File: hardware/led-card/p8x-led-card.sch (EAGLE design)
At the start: 19 parts, among them J1 MABC96R, U1 74HCT30, U2 74HCT138, U3 74HCT138, U4 74HCT32, U5 74HCT14, U6 74HCT374

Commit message: feat(hardware): 100nF bypass caps to 0.1" lead pitch on all boards
The 100nF ceramic-disc decoupling/bypass caps used the shared C_DISC footprint
at 0.2" (5.08mm) lead spacing. The parts being sourced are 0.1" (2.54mm) pitch,
so retarget just those caps:

- Add a C_DISC1 footprint (pad 2 at y=-2.54) and a CAP1 device that reuses the
  CAP schematic symbol art but points at C_DISC1.
- Route the 100nF parts to CAP1: per-IC decoupling (CDn), the placement-flow
  copies, and the backplane per-slot caps C1-C10.
- Leave C_DISC (0.2") for the parts that still use it: the 1uF caps, the 150pF
  clock terminators (CT1/CT2), and the XTAL32 placeholder.

Regenerated all 8 boards (.sch/.brd/-full.brd) and the schematic PDFs; the
narrower pad field also relieves the backplane connector clearance. Validation:
0 errors on all boards.

Co-Authored-By: Claude Opus 4.8 <noreply@anthropic.com>
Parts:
- CD1, CD2, CD3, CD4, CD5, CD6: device p8x:CAP -> p8x:CAP1
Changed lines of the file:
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@@
 <part name="R4" library="p8x" deviceset="RES" device="" value="1K"/>
 <part name="LED4" library="p8x" deviceset="LED" device="" value="YEL"/>
-<part name="CD1" library="p8x" deviceset="CAP" device="" value="100N"/>
-<part name="CD2" library="p8x" deviceset="CAP" device="" value="100N"/>
-<part name="CD3" library="p8x" deviceset="CAP" device="" value="100N"/>
-<part name="CD4" library="p8x" deviceset="CAP" device="" value="100N"/>
-<part name="CD5" library="p8x" deviceset="CAP" device="" value="100N"/>
-<part name="CD6" library="p8x" deviceset="CAP" device="" value="100N"/>
+<part name="CD1" library="p8x" deviceset="CAP1" device="" value="100N"/>
+<part name="CD2" library="p8x" deviceset="CAP1" device="" value="100N"/>
+<part name="CD3" library="p8x" deviceset="CAP1" device="" value="100N"/>
+<part name="CD4" library="p8x" deviceset="CAP1" device="" value="100N"/>
+<part name="CD5" library="p8x" deviceset="CAP1" device="" value="100N"/>
+<part name="CD6" library="p8x" deviceset="CAP1" device="" value="100N"/>
 </parts><sheets><sheet><plain>
 <text x="0" y="40" size="3.81" layer="97">P8X LED OUTPUT CARD (test - write-only 8 LEDs at $FF0C)</text>

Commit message: fix(gen_eagle): card J1 schematic footprint was FABC96S (female), should be MABC96R
Spotted on the bustest board review: J1, the card edge connector, showed as
FABC96S in the schematic — the female VERTICAL backplane socket — when a card
mates as the MALE right-angle MABC96R. card() bound the schematic J1 to deviceset
DIN96 (FABC96S) while the board bound DIN96C (MABC96R): a schematic/board
footprint mismatch present on EVERY card, not just bustest.

The physical result was never wrong — the generator bakes identical pad geometry
for both names (verified: MABC96R and FABC96S have byte-identical pad maps in
con-vg too), so boards were always correct. But the schematic labelled the card
connector as the backplane socket, which is what the review caught, and it breaks
schematic/board consistency.

One-line fix: schematic J1 now binds DIN96C -> MABC96R, matching the board. The
backplane keeps DIN96/FABC96S for its own slots — those ARE the female sockets;
only cards are male. All 8 existing card schematics get the same correction (they
shared the bug); the backplane schematic and every .brd are unchanged.

Regenerated the 9 affected schematic PDFs to match; reverted placement-PDF and
backplane-PDF timestamp churn.

Co-Authored-By: Claude Opus 4.8 <noreply@anthropic.com>
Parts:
- J1: device p8x:DIN96 -> p8x:DIN96C
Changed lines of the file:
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@@
 <classes><class number="0" name="default" width="0" drill="0"/></classes>
 <parts>
-<part name="J1" library="p8x" deviceset="DIN96" device="" value="MABC96R"/>
+<part name="J1" library="p8x" deviceset="DIN96C" device="" value="MABC96R"/>
 <part name="U1" library="p8x" deviceset="7430" device="" value="74HCT30"/>
 <part name="U2" library="p8x" deviceset="74138" device="" value="74HCT138"/>

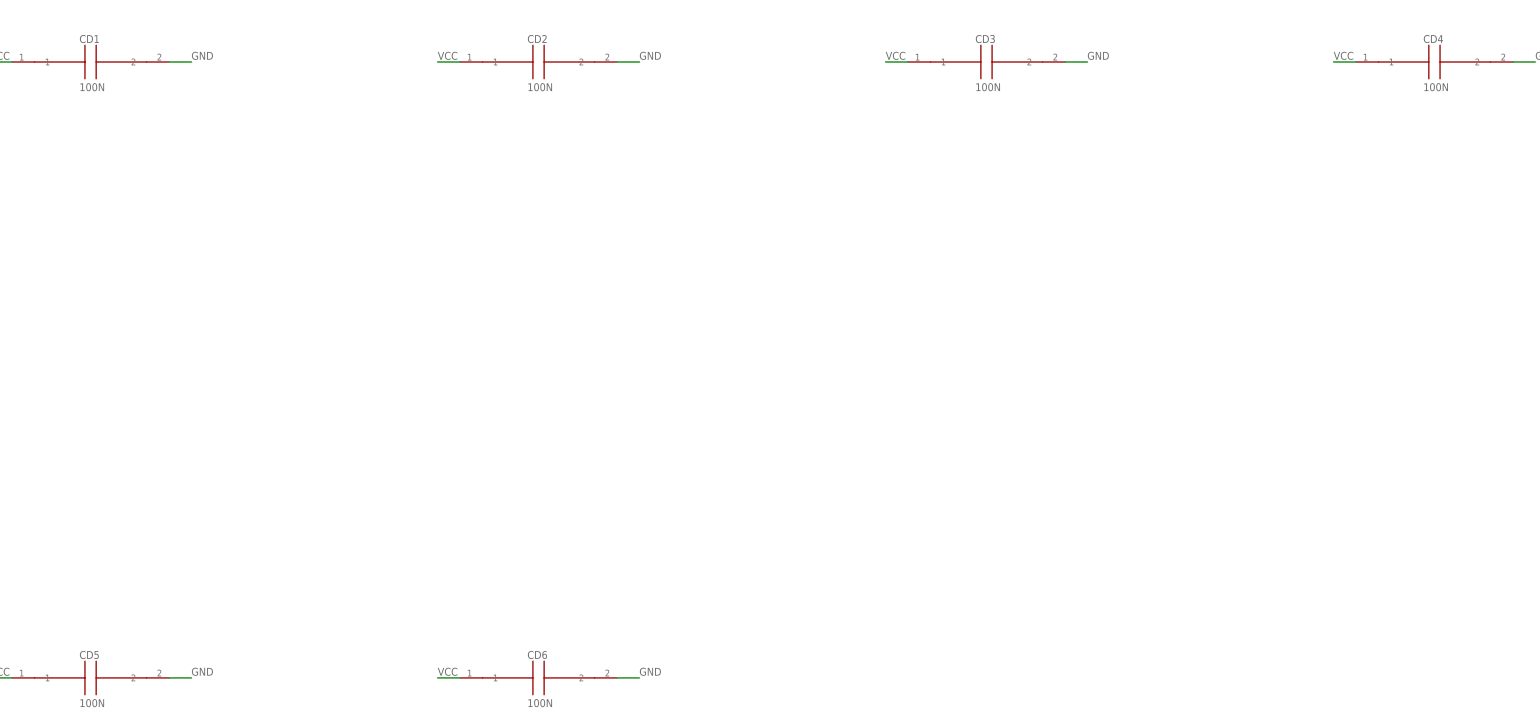
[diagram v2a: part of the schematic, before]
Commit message: hardware: silkscreen off footprints, standard cap value format, backplane RL1->R1
Pre-Fusion cleanup so there is less to fix by hand once placing/routing.

1. SILKSCREEN NO LONGER OVERLAYS FOOTPRINTS (all boards). NAME/VALUE were emitted
   at the element origin +/-2.54 regardless of part size, so on anything bigger
   than a 2-pin part the text landed ON the pads -- the 96-pin DIN connector had
   J1/SLOT1 across its pad field, and caps had their values on top of them. Now
   placed against the real footprint bbox (fp_box): NAME 0.7mm above the top edge,
   VALUE 0.7mm below the bottom, left-aligned to the box. Verified: 1642
   silkscreen labels across all 9 boards, 0 sitting on a footprint (was many).
   Not rotation-aware, which is fine -- no board rotates a part today.

2. CAPACITOR VALUES use standard unit suffixes: 100N->100nF, 470U->470uF,
   150P->150pF, 1U->1uF (and the DNP/x10 variants). Applied everywhere, so the
   per-IC decoupling caps on every card change too. No doc quoted the raw value
   strings, so no doc churn.

3. BACKPLANE RL1 -> R1 (standard R designator). Scoped to the backplane section
   only -- the io-card and led-card have their own unrelated RL1 (8x330R networks)
   which are untouched. Backplane theory/design docs updated to match.

Part refs/values are decided in gen_eagle.py: the backplane `small=[...]` list and
each cards `ic`/`sm` dicts.

Co-Authored-By: Claude Opus 4.8 <noreply@anthropic.com>
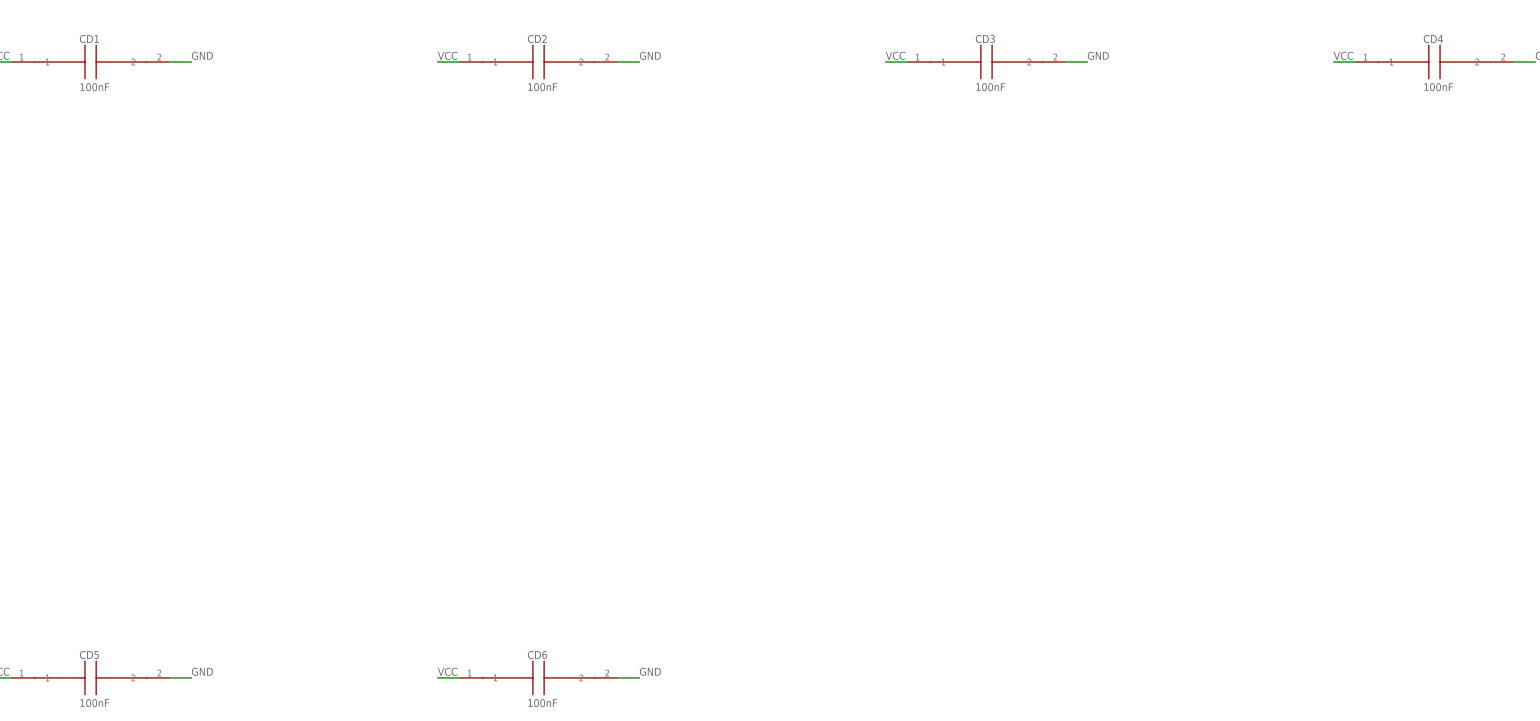
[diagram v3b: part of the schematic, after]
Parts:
- CD1, CD2, CD3, CD4, CD5, CD6: value 100N -> 100nF
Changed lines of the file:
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@@
 <part name="R4" library="p8x" deviceset="RES" device="" value="1K"/>
 <part name="LED4" library="p8x" deviceset="LED" device="" value="YEL"/>
-<part name="CD1" library="p8x" deviceset="CAP1" device="" value="100N"/>
-<part name="CD2" library="p8x" deviceset="CAP1" device="" value="100N"/>
-<part name="CD3" library="p8x" deviceset="CAP1" device="" value="100N"/>
-<part name="CD4" library="p8x" deviceset="CAP1" device="" value="100N"/>
-<part name="CD5" library="p8x" deviceset="CAP1" device="" value="100N"/>
-<part name="CD6" library="p8x" deviceset="CAP1" device="" value="100N"/>
+<part name="CD1" library="p8x" deviceset="CAP1" device="" value="100nF"/>
+<part name="CD2" library="p8x" deviceset="CAP1" device="" value="100nF"/>
+<part name="CD3" library="p8x" deviceset="CAP1" device="" value="100nF"/>
+<part name="CD4" library="p8x" deviceset="CAP1" device="" value="100nF"/>
+<part name="CD5" library="p8x" deviceset="CAP1" device="" value="100nF"/>
+<part name="CD6" library="p8x" deviceset="CAP1" device="" value="100nF"/>
 </parts><sheets><sheet><plain>
 <text x="0" y="40" size="3.81" layer="97">P8X LED OUTPUT CARD (test - write-only 8 LEDs at $FF0C)</text>

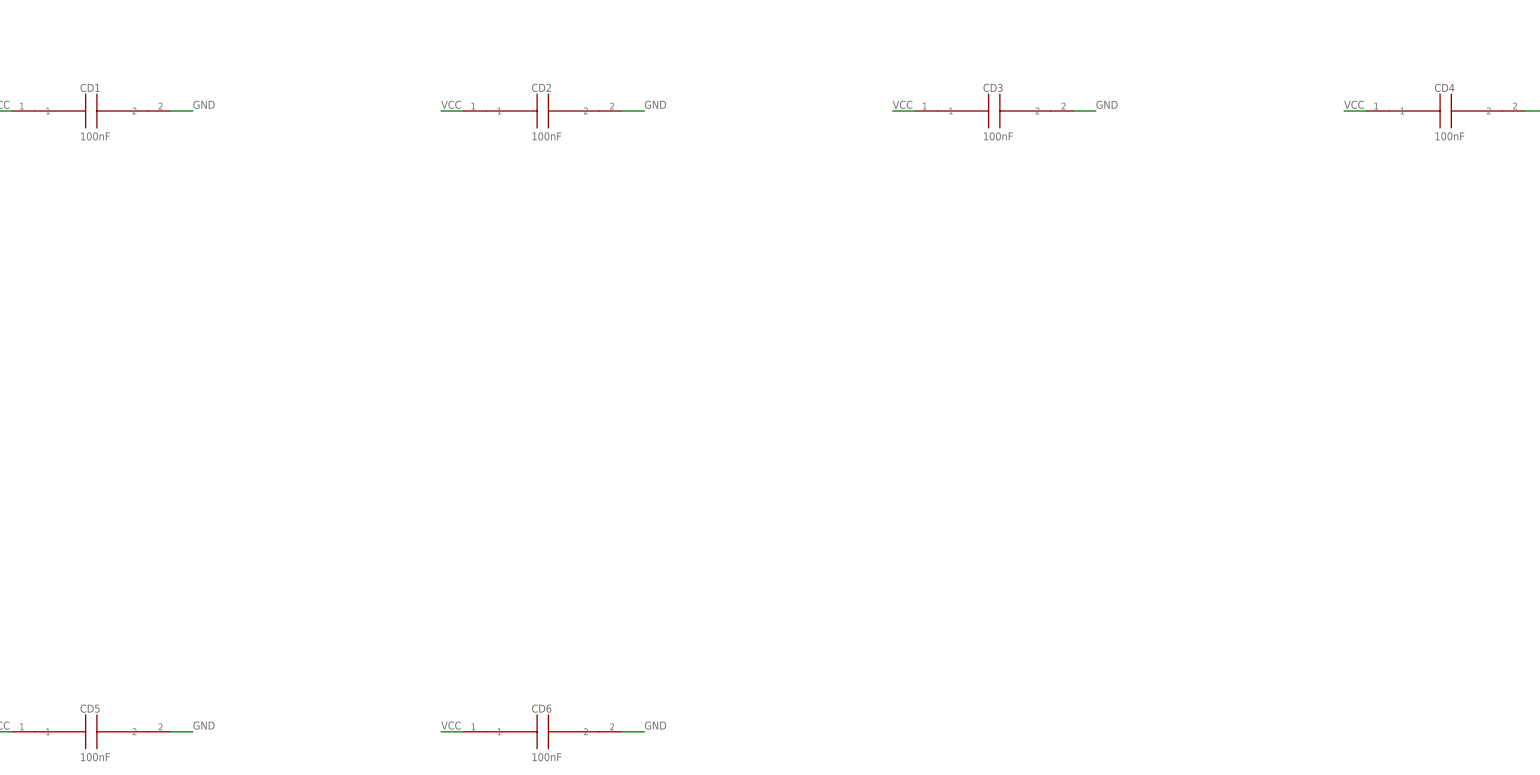
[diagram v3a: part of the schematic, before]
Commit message: refactor(ecad): decoupling caps use C designator, not CD
Per-IC decoupling caps were named CD1..CDn (a "CD" prefix chosen long ago to
dodge functional Cn caps). Renamed to plain Cn, matching the backplane (which
already uses C1..C14) and standard practice.

Collisions handled by numbering the decoupling block AFTER the highest
functional C on each card:
  - io-card keeps functional C2-C5; decoupling continues C6-C21
  - control-card keeps functional C1; decoupling C2-C22
  - every other card has no functional Cn, so decoupling is C1..Cn
Cards with no functional caps keep the same numbers they had (memory CD11 ->
C11, etc.), so those doc references are a pure CD->C rename.

Designator-only change: verified the board diffs touch no wire/via/package/
coordinate lines (equal insert/delete counts are the rename). Stale CDn mentions
in gen_eagle comments and the memory-card theory/README updated. All 9 boards
validate; no CDn left in the tree.

Co-Authored-By: Claude Opus 4.8 <noreply@anthropic.com>
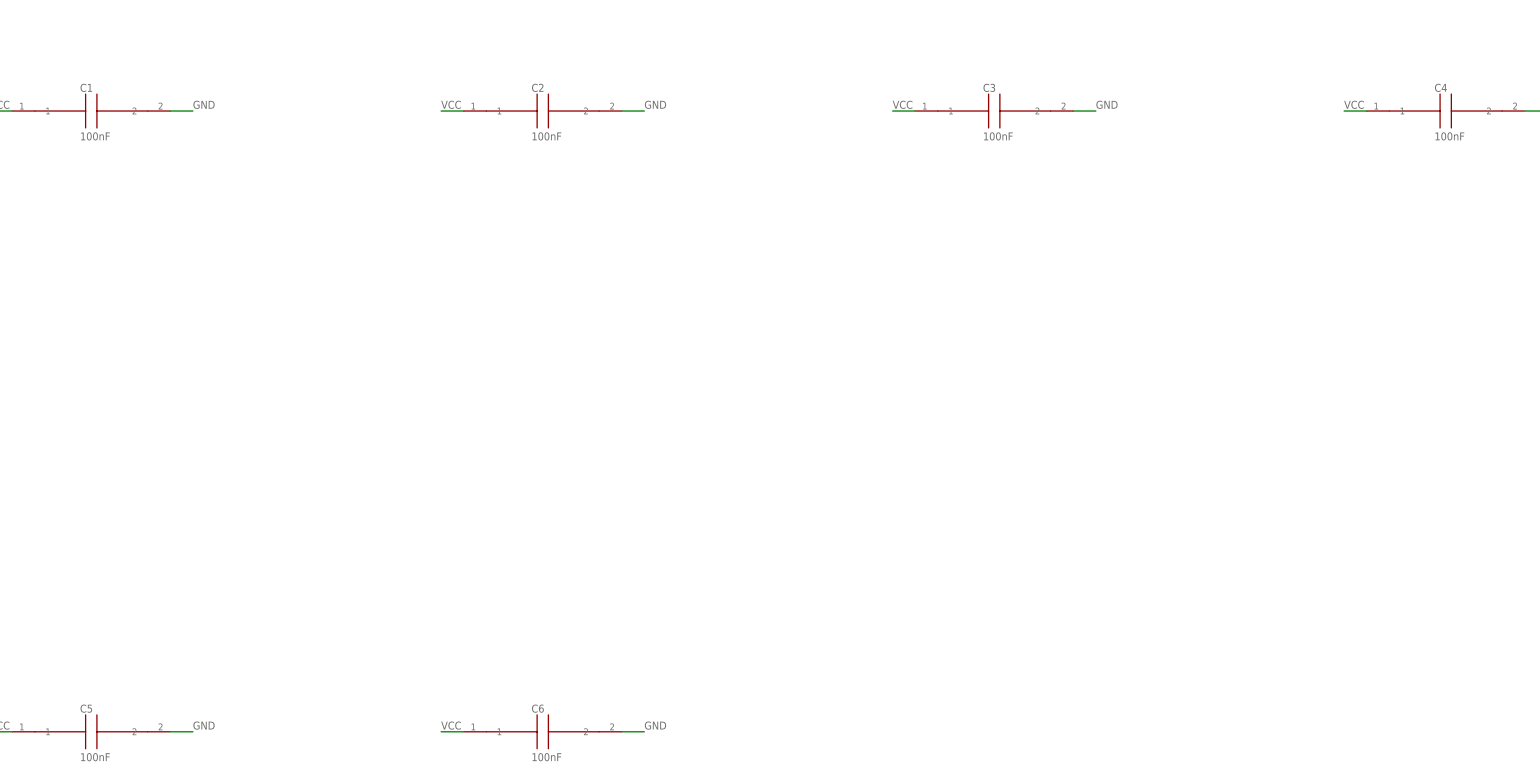
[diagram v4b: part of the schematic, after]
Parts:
- renumbered CD1 to C1, CD2 to C2, CD3 to C3, CD4 to C4, CD5 to C5, CD6 to C6
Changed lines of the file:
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@@
 <part name="R4" library="p8x" deviceset="RES" device="" value="1K"/>
 <part name="LED4" library="p8x" deviceset="LED" device="" value="YEL"/>
-<part name="CD1" library="p8x" deviceset="CAP1" device="" value="100nF"/>
-<part name="CD2" library="p8x" deviceset="CAP1" device="" value="100nF"/>
-<part name="CD3" library="p8x" deviceset="CAP1" device="" value="100nF"/>
-<part name="CD4" library="p8x" deviceset="CAP1" device="" value="100nF"/>
-<part name="CD5" library="p8x" deviceset="CAP1" device="" value="100nF"/>
-<part name="CD6" library="p8x" deviceset="CAP1" device="" value="100nF"/>
+<part name="C1" library="p8x" deviceset="CAP1" device="" value="100nF"/>
+<part name="C2" library="p8x" deviceset="CAP1" device="" value="100nF"/>
+<part name="C3" library="p8x" deviceset="CAP1" device="" value="100nF"/>
+<part name="C4" library="p8x" deviceset="CAP1" device="" value="100nF"/>
+<part name="C5" library="p8x" deviceset="CAP1" device="" value="100nF"/>
+<part name="C6" library="p8x" deviceset="CAP1" device="" value="100nF"/>
 </parts><sheets><sheet><plain>
 <text x="0" y="40" size="3.81" layer="97">P8X LED OUTPUT CARD (test - write-only 8 LEDs at $FF0C)</text>
@@
 <instance part="R4" gate="G$1" x="343.2" y="-241.29999999999998"/>
 <instance part="LED4" gate="G$1" x="444.79999999999995" y="-241.29999999999998"/>
-<instance part="CD1" gate="G$1" x="140.0" y="-380.99999999999994"/>
-<instance part="CD2" gate="G$1" x="241.6" y="-380.99999999999994"/>
-<instance part="CD3" gate="G$1" x="343.2" y="-380.99999999999994"/>
-<instance part="CD4" gate="G$1" x="444.79999999999995" y="-380.99999999999994"/>
-<instance part="CD5" gate="G$1" x="140.0" y="-520.6999999999999"/>
-<instance part="CD6" gate="G$1" x="241.6" y="-520.6999999999999"/>
+<instance part="C1" gate="G$1" x="140.0" y="-380.99999999999994"/>
+<instance part="C2" gate="G$1" x="241.6" y="-380.99999999999994"/>
+<instance part="C3" gate="G$1" x="343.2" y="-380.99999999999994"/>
+<instance part="C4" gate="G$1" x="444.79999999999995" y="-380.99999999999994"/>
+<instance part="C5" gate="G$1" x="140.0" y="-520.6999999999999"/>
+<instance part="C6" gate="G$1" x="241.6" y="-520.6999999999999"/>
 </instances><busses/><nets>
 <net name="A8" class="0">
@@
 <wire x1="17.78" y1="35.56" x2="22.86" y2="35.56" width="0.1524" layer="91"/>
 <label x="22.86" y="36.07" size="1.778" layer="95"/></segment>
-<segment><pinref part="CD1" gate="G$1" pin="1"/>
+<segment><pinref part="C1" gate="G$1" pin="1"/>
 <wire x1="122.22" y1="-381.00" x2="117.14" y2="-381.00" width="0.1524" layer="91"/>
 <label x="117.14" y="-380.49" size="1.778" layer="95"/></segment>
-<segment><pinref part="CD2" gate="G$1" pin="1"/>
+<segment><pinref part="C2" gate="G$1" pin="1"/>
 <wire x1="223.82" y1="-381.00" x2="218.74" y2="-381.00" width="0.1524" layer="91"/>
 <label x="218.74" y="-380.49" size="1.778" layer="95"/></segment>
-<segment><pinref part="CD3" gate="G$1" pin="1"/>
+<segment><pinref part="C3" gate="G$1" pin="1"/>
 <wire x1="325.42" y1="-381.00" x2="320.34" y2="-381.00" width="0.1524" layer="91"/>
 <label x="320.34" y="-380.49" size="1.778" layer="95"/></segment>
-<segment><pinref part="CD4" gate="G$1" pin="1"/>
+<segment><pinref part="C4" gate="G$1" pin="1"/>
 <wire x1="427.02" y1="-381.00" x2="421.94" y2="-381.00" width="0.1524" layer="91"/>
 <label x="421.94" y="-380.49" size="1.778" layer="95"/></segment>
-<segment><pinref part="CD5" gate="G$1" pin="1"/>
+<segment><pinref part="C5" gate="G$1" pin="1"/>
 <wire x1="122.22" y1="-520.70" x2="117.14" y2="-520.70" width="0.1524" layer="91"/>
 <label x="117.14" y="-520.19" size="1.778" layer="95"/></segment>
-<segment><pinref part="CD6" gate="G$1" pin="1"/>
+<segment><pinref part="C6" gate="G$1" pin="1"/>
 <wire x1="223.82" y1="-520.70" x2="218.74" y2="-520.70" width="0.1524" layer="91"/>
 <label x="218.74" y="-520.19" size="1.778" layer="95"/></segment>
@@
 <wire x1="17.78" y1="-40.64" x2="22.86" y2="-40.64" width="0.1524" layer="91"/>
 <label x="22.86" y="-40.13" size="1.778" layer="95"/></segment>
-<segment><pinref part="CD1" gate="G$1" pin="2"/>
+<segment><pinref part="C1" gate="G$1" pin="2"/>
 <wire x1="157.78" y1="-381.00" x2="162.86" y2="-381.00" width="0.1524" layer="91"/>
 <label x="162.86" y="-380.49" size="1.778" layer="95"/></segment>
-<segment><pinref part="CD2" gate="G$1" pin="2"/>
+<segment><pinref part="C2" gate="G$1" pin="2"/>
 <wire x1="259.38" y1="-381.00" x2="264.46" y2="-381.00" width="0.1524" layer="91"/>
 <label x="264.46" y="-380.49" size="1.778" layer="95"/></segment>
-<segment><pinref part="CD3" gate="G$1" pin="2"/>
+<segment><pinref part="C3" gate="G$1" pin="2"/>
 <wire x1="360.98" y1="-381.00" x2="366.06" y2="-381.00" width="0.1524" layer="91"/>
 <label x="366.06" y="-380.49" size="1.778" layer="95"/></segment>
-<segment><pinref part="CD4" gate="G$1" pin="2"/>
+<segment><pinref part="C4" gate="G$1" pin="2"/>
 <wire x1="462.58" y1="-381.00" x2="467.66" y2="-381.00" width="0.1524" layer="91"/>
 <label x="467.66" y="-380.49" size="1.778" layer="95"/></segment>
-<segment><pinref part="CD5" gate="G$1" pin="2"/>
+<segment><pinref part="C5" gate="G$1" pin="2"/>
 <wire x1="157.78" y1="-520.70" x2="162.86" y2="-520.70" width="0.1524" layer="91"/>
 <label x="162.86" y="-520.19" size="1.778" layer="95"/></segment>
-<segment><pinref part="CD6" gate="G$1" pin="2"/>
+<segment><pinref part="C6" gate="G$1" pin="2"/>
 <wire x1="259.38" y1="-520.70" x2="264.46" y2="-520.70" width="0.1524" layer="91"/>
 <label x="264.46" y="-520.19" size="1.778" layer="95"/></segment>
